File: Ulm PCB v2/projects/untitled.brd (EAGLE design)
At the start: 39.4 x 49.5 mm, 26 parts, among them U1 FT232RLSSOP, U2 MCP73831, U3 SPX3819-3.3, X2 USB-SMD-NS

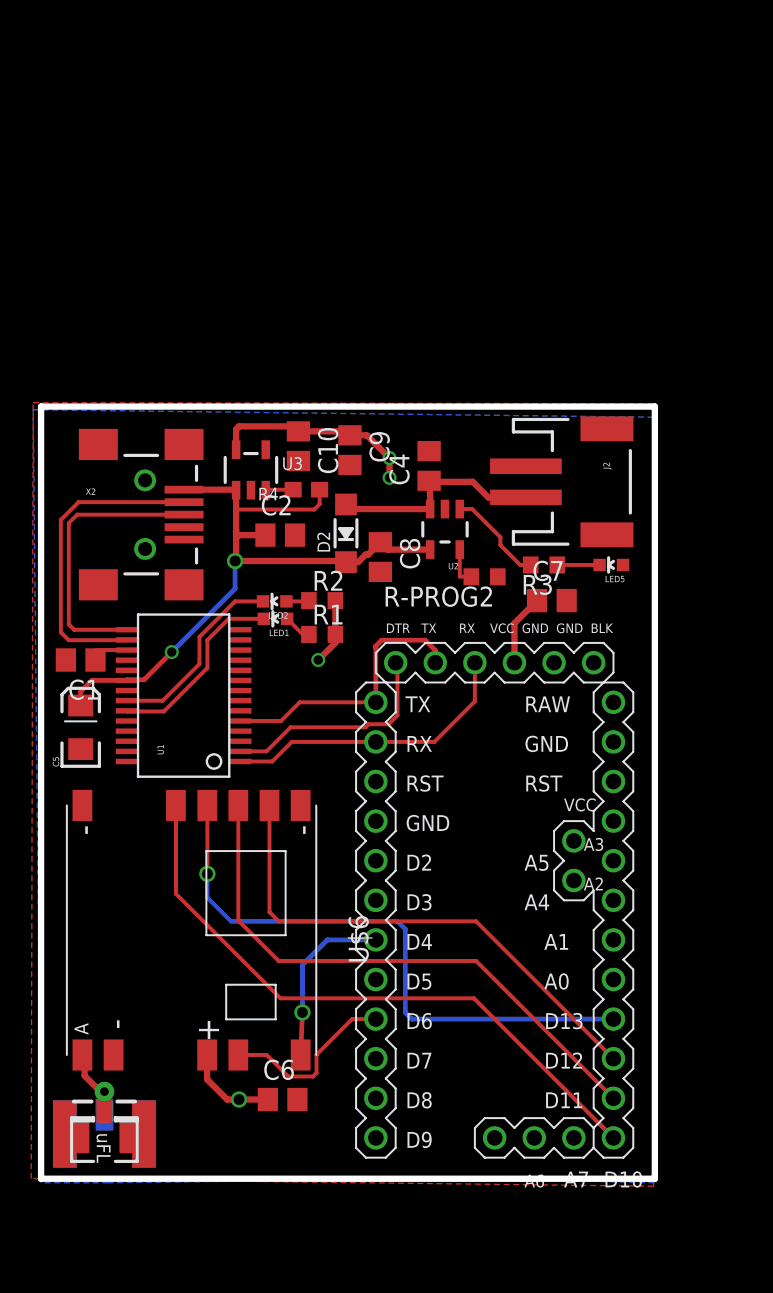
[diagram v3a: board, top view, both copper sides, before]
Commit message: added picture of board layout
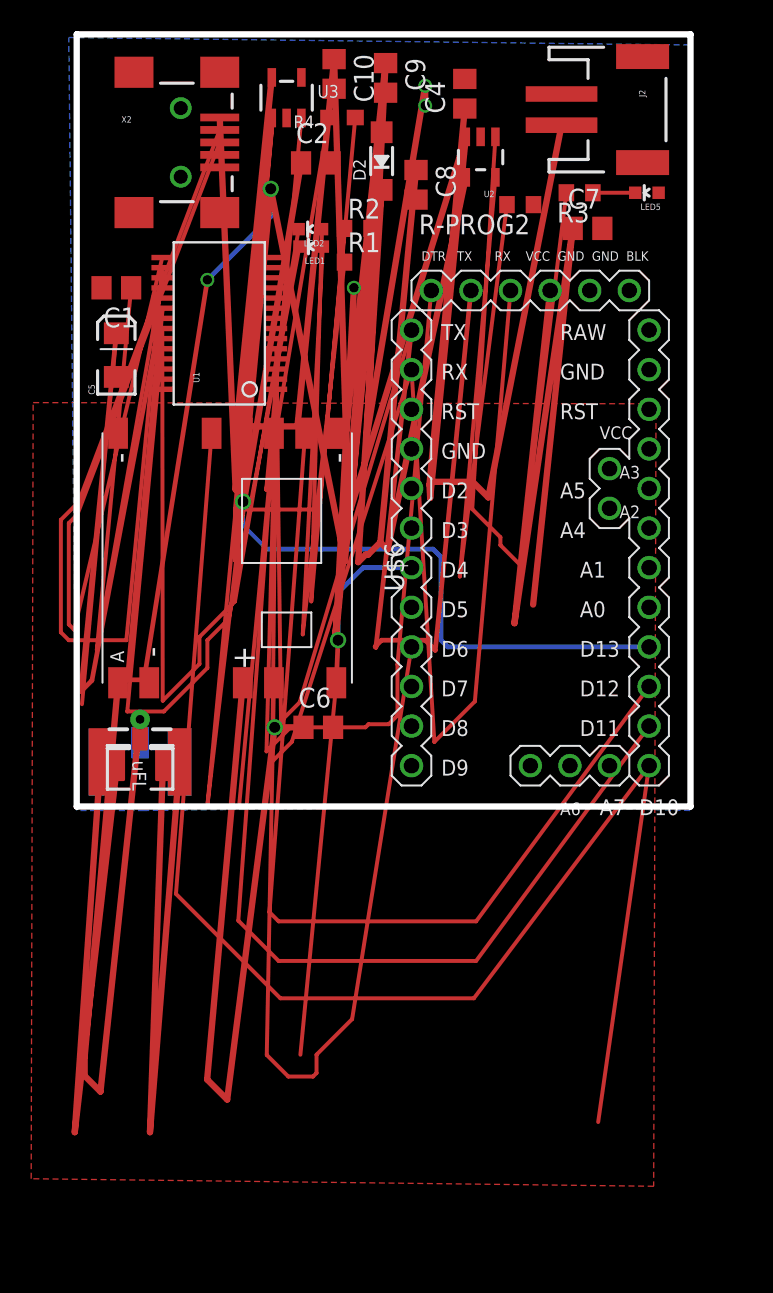
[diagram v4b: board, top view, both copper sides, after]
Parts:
- moved C10 24.0 mm to (18.8, 83.6)
- moved C4 24.0 mm to (27.2, 82.3)
- moved J$2 24.0 mm to (6.35, 37.1)
- moved LED1 24.0 mm to (17.3, 72.5)
- moved LED2 24.0 mm to (17.3, 73.6)
- moved R4 24.0 mm to (19.3, 80.8)
- moved U3 24.0 mm to (15.7, 82.0)
- moved U$6 24.0 mm to (11.9, 50.3)
- moved C1 24.0 mm to (4.83, 69.8)
- moved C2 24.0 mm to (17.6, 77.9)
- moved C5 24.0 mm to (4.83, 65.5)
- moved C6 24.0 mm to (17.8, 41.7)
- moved C7 24.0 mm to (35.1, 73.7)
- moved C9 24.0 mm to (22.1, 83.3)
- moved D2 24.0 mm to (21.8, 78.0)
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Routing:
- net 5V: track 45.1 -> 409.1 mm
- net 3.3V: track 28.7 -> 368.0 mm
- net VBAT: track 14.0 -> 126.2 mm
- net GND: track 3.03 -> 95.0 mm
- net TXO: track 19.1 -> 104.8 mm
- net RXI: track 17.9 -> 98.5 mm
- net MOSI: track 36.2 -> 90.4 mm
- net CS: track 41.6 -> 93.3 mm
- net N$4: track 5.81 -> 53.5 mm
- net LOL: track 2.47 -> 49.7 mm
- net N$1: track 1.80 -> 48.9 mm
- net N$6: track 6.33 -> 52.8 mm
- net EN: track 1.77 -> 48.2 mm
- net DTR: track 14.4 -> 60.6 mm
- net N$2: track 1.76 -> 47.9 mm
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
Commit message: Revert "added picture of board layout"
This reverts commit 6c2dd7b23edb37982c4fb7cb2418e2451a8ef545.
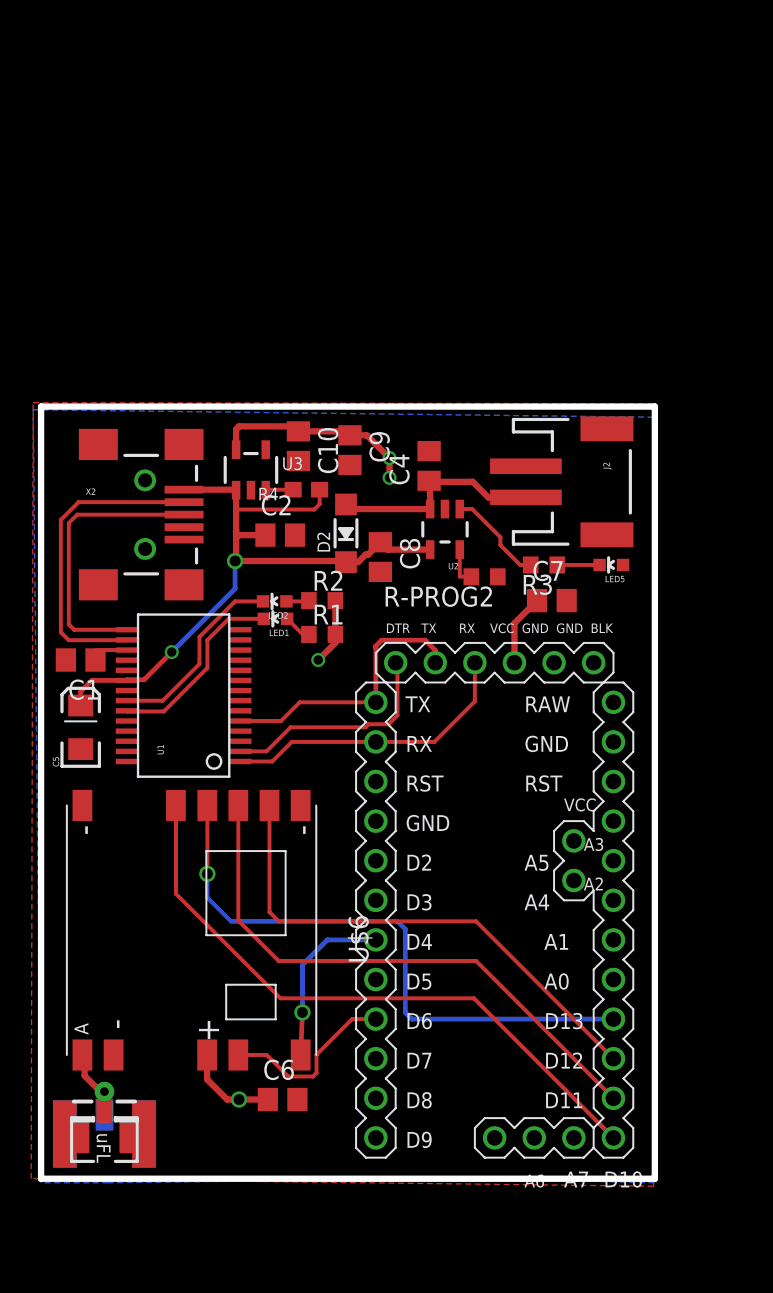
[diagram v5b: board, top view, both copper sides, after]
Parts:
- moved C10 24.0 mm to (16.5, 59.7)
- moved C4 24.0 mm to (24.9, 58.4)
- moved J$2 24.0 mm to (4.06, 13.2)
- moved LED1 24.0 mm to (15.0, 48.6)
- moved LED2 24.0 mm to (15.0, 49.7)
- moved R4 24.0 mm to (17.0, 56.9)
- moved U3 24.0 mm to (13.5, 58.2)
- moved U$6 24.0 mm to (9.65, 26.4)
- moved C1 24.0 mm to (2.54, 46.0)
- moved C2 24.0 mm to (15.3, 54.0)
- moved C5 24.0 mm to (2.54, 41.7)
- moved C6 24.0 mm to (15.5, 17.8)
- moved C7 24.0 mm to (32.8, 49.8)
- moved C9 24.0 mm to (19.8, 59.4)
- moved D2 24.0 mm to (19.6, 54.1)
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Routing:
- net 5V: track 409.1 -> 45.1 mm
- net 3.3V: track 368.0 -> 28.7 mm
- net VBAT: track 126.2 -> 14.0 mm
- net GND: track 95.0 -> 3.03 mm
- net TXO: track 104.8 -> 19.1 mm
- net RXI: track 98.5 -> 17.9 mm
- net MOSI: track 90.4 -> 36.2 mm
- net CS: track 93.3 -> 41.6 mm
- net N$4: track 53.5 -> 5.81 mm
- net LOL: track 49.7 -> 2.47 mm
- net N$1: track 48.9 -> 1.80 mm
- net N$6: track 52.8 -> 6.33 mm
- net EN: track 48.2 -> 1.77 mm
- net DTR: track 60.6 -> 14.4 mm
- net N$2: track 47.9 -> 1.76 mm
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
